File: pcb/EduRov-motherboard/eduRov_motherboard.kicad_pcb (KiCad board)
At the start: 4 copper layers, 167.7 x 124.6 mm, 65 parts, among them IC201 L6203, IC301 L6203, IC401 L6203, IC501 L6203, P101 Battery connector, P102 Ext press, P103 Ext press, P104 Ext press, P105 Ch LED, Q101 IRL540NPBF, U201 ACS723xLCTR-05AB, U301 ACS723xLCTR-05AB, U401 ACS723xLCTR-05AB, U501 ACS723xLCTR-05AB

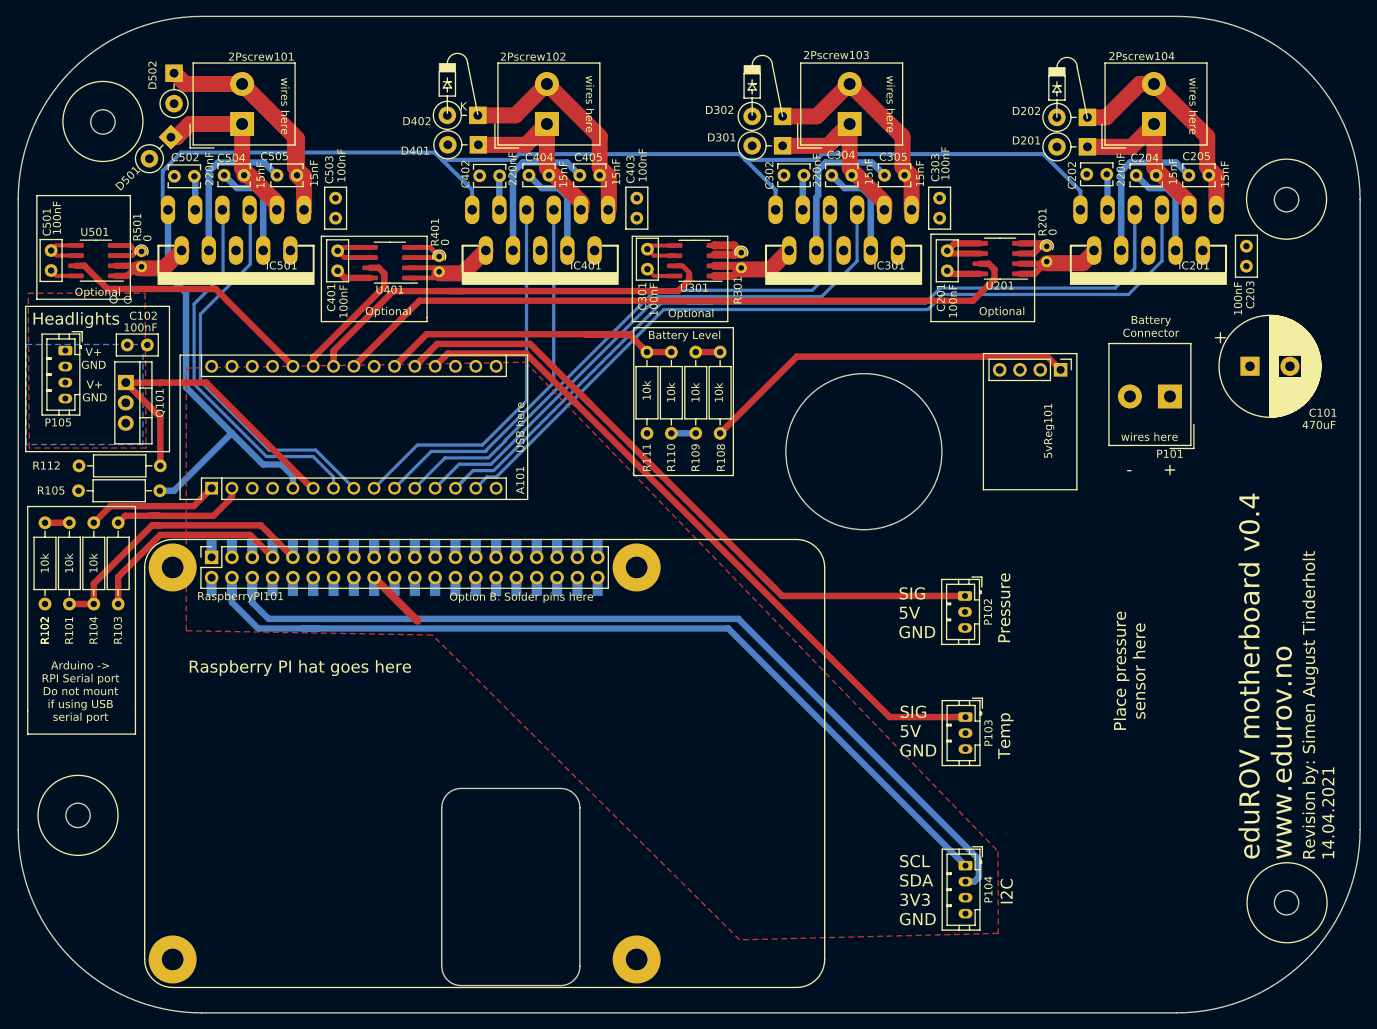
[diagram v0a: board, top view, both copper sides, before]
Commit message: Use L298 motor driver
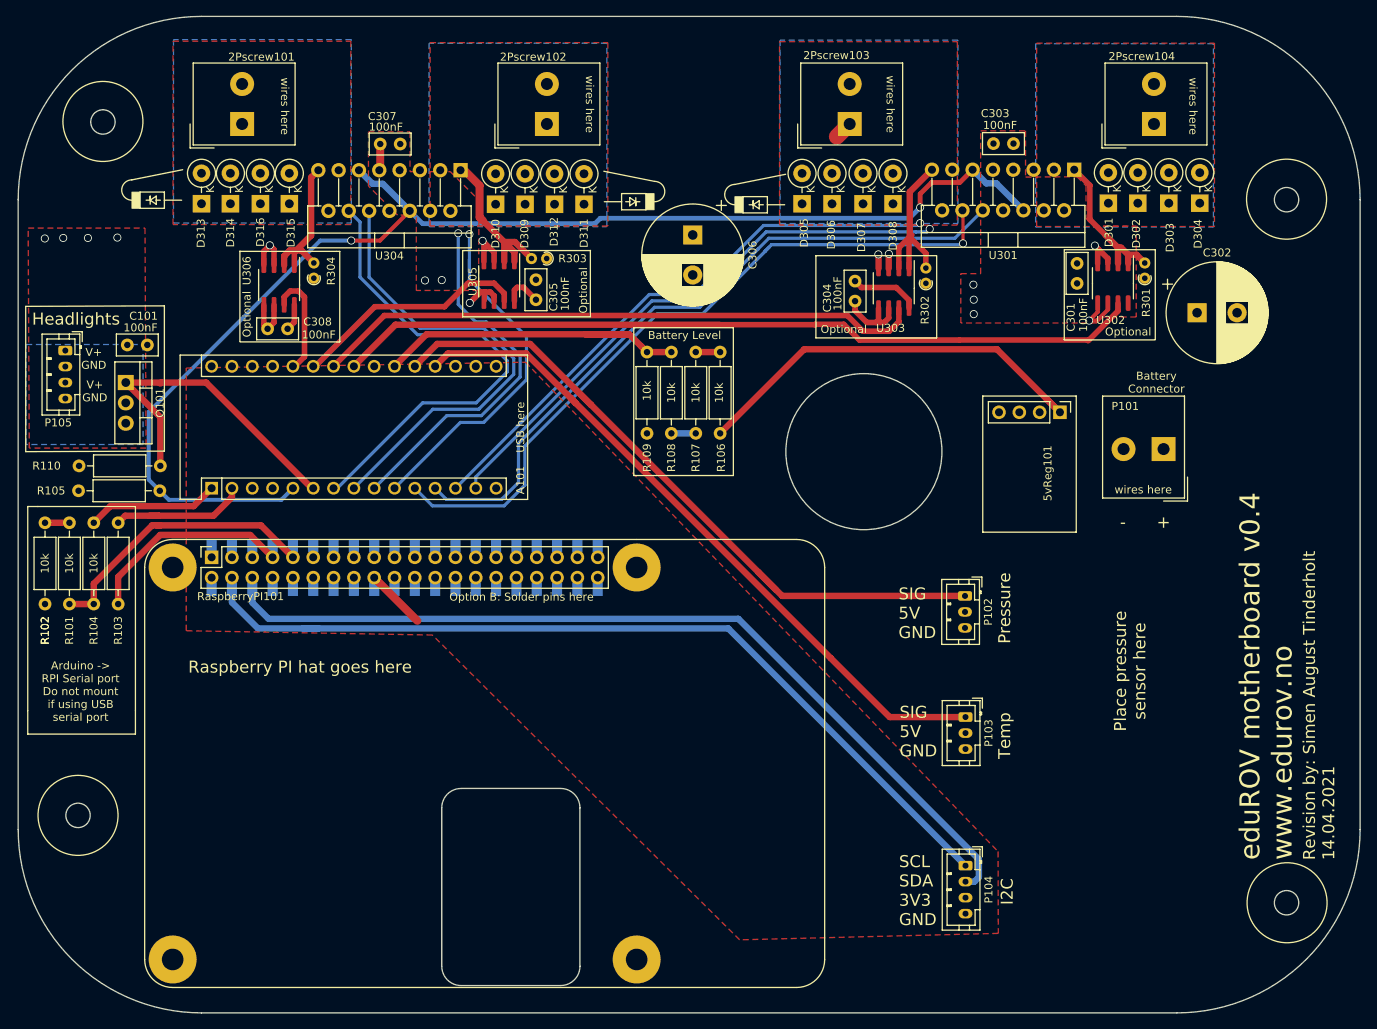
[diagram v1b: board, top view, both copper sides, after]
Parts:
- removed the C101 at (209.8, 76.7)
- removed C201, C203, C401, C403, C501, C503: 100nF, Capacitor_THT:C_Disc_D5.0mm_W2.5mm_P2.50mm
- removed C202, C402, C502: 220nF, Capacitor_THT:C_Disc_D3.8mm_W2.6mm_P2.50mm
- removed C204, C205, C404, C405, C504, C505: 15nF, Capacitor_THT:C_Disc_D3.8mm_W2.6mm_P2.50mm
- removed D201, D202, D401, D402, D501, D502: D, Diode_THT:D_DO-41_SOD81_P3.81mm_Vertical_KathodeUp
- removed IC201, IC301, IC401, IC501: L6203, SnapEDA Library:MULTIWATT-11
- removed R201, R401, R501: 0, Resistor_THT:R_Axial_DIN0204_L3.6mm_D1.6mm_P1.90mm_Vertical
- removed U201, U401, U501: ACS723xLCTR-05AB, Package_SO:SOIC-8_3.9x4.9mm_P1.27mm
- added C306: 470uF, Capacitor_THT:CP_Radial_D12.5mm_P5.00mm, F.Cu at (140.1, 60.3)
- added C307: 100nF, Capacitor_THT:C_Disc_D5.0mm_W2.5mm_P2.50mm, F.Cu at (103.6, 48.9)
- added C308: 100nF, Capacitor_THT:C_Disc_D5.0mm_W2.5mm_P2.50mm, F.Cu at (87.0, 72.0)
- added D303: D, Diode_THT:D_DO-41_SOD81_P3.81mm_Vertical_KathodeUp, F.Cu at (199.7, 56.3)
- added D304: D, Diode_THT:D_DO-41_SOD81_P3.81mm_Vertical_KathodeUp, F.Cu at (203.5, 56.3)
- added D305: D, Diode_THT:D_DO-41_SOD81_P3.81mm_Vertical_KathodeUp, F.Cu at (153.8, 56.4)
- added D306: D, Diode_THT:D_DO-41_SOD81_P3.81mm_Vertical_KathodeUp, F.Cu at (157.6, 56.4)
- added D307: D, Diode_THT:D_DO-41_SOD81_P3.81mm_Vertical_KathodeUp, F.Cu at (161.4, 56.4)
- added D308: D, Diode_THT:D_DO-41_SOD81_P3.81mm_Vertical_KathodeUp, F.Cu at (165.2, 56.4)
- added D309: D, Diode_THT:D_DO-41_SOD81_P3.81mm_Vertical_KathodeUp, F.Cu at (119.2, 56.5)
- added D310: D, Diode_THT:D_DO-41_SOD81_P3.81mm_Vertical_KathodeUp, F.Cu at (115.5, 56.5)
- added D311: D, Diode_THT:D_DO-41_SOD81_P3.81mm_Vertical_KathodeUp, F.Cu at (126.6, 56.5)
- added D312: D, Diode_THT:D_DO-41_SOD81_P3.81mm_Vertical_KathodeUp, F.Cu at (122.9, 56.5)
- added D313: D, Diode_THT:D_DO-41_SOD81_P3.81mm_Vertical_KathodeUp, F.Cu at (78.7, 56.4)
- added D314: D, Diode_THT:D_DO-41_SOD81_P3.81mm_Vertical_KathodeUp, F.Cu at (82.4, 56.4)
- added D315: D, Diode_THT:D_DO-41_SOD81_P3.81mm_Vertical_KathodeUp, F.Cu at (89.7, 56.4)
- added D316: D, Diode_THT:D_DO-41_SOD81_P3.81mm_Vertical_KathodeUp, F.Cu at (86.1, 56.4)
- added R302: 0, Resistor_THT:R_Axial_DIN0204_L3.6mm_D1.6mm_P1.90mm_Vertical, F.Cu at (169.3, 66.3)
- added R303: 0, Resistor_THT:R_Axial_DIN0204_L3.6mm_D1.6mm_P1.90mm_Vertical, F.Cu at (121.9, 63.2)
- added R304: 0, Resistor_THT:R_Axial_DIN0204_L3.6mm_D1.6mm_P1.90mm_Vertical, F.Cu at (92.8, 65.7)
- added U302: ACS723xLCTR-05AB, Package_SO:SOIC-8_3.9x4.9mm_P1.27mm, F.Cu at (192.7, 66.3)
- added U303: ACS723xLCTR-05AB, Package_SO:SOIC-8_3.9x4.9mm_P1.27mm, F.Cu at (165.3, 67.0)
- added U304: L298HN, Package_TO_SOT_THT:TO-220-15_P2.54x2.54mm_StaggerOdd_Lead4.58mm_Vertical, F.Cu at (111.1, 52.2)
- added U305: ACS723xLCTR-05AB, Package_SO:SOIC-8_3.9x4.9mm_P1.27mm, F.Cu at (116.0, 66.1)
- added U306: ACS723xLCTR-05AB, Package_SO:SOIC-8_3.9x4.9mm_P1.27mm, F.Cu at (88.4, 66.5)
- C302: value 220nF -> 470uF; footprint Capacitor_THT:C_Disc_D3.8mm_W2.6mm_P2.50mm -> Capacitor_THT:CP_Radial_D12.5mm_P5.00mm
- C304, C305: value 15nF -> 100nF; footprint Capacitor_THT:C_Disc_D3.8mm_W2.6mm_P2.50mm -> Capacitor_THT:C_Disc_D5.0mm_W2.5mm_P2.50mm
- U301: value ACS723xLCTR-05AB -> L298HN; footprint Package_SO:SOIC-8_3.9x4.9mm_P1.27mm -> Package_TO_SOT_THT:TO-220-15_P2.54x2.54mm_StaggerOdd_Lead4.58mm_Vertical
- moved C301 53.9 mm to (188.2, 66.3), turned to 90 degrees
- moved C302 52.1 mm to (203.2, 70.0), turned to 0 degrees
- moved R301 50.5 mm to (196.7, 65.7), turned to 90 degrees
- moved U301 48.8 mm to (187.8, 52.1)
- moved C305 47.9 mm to (120.5, 65.9), turned to 270 degrees
- moved D302 45.7 mm to (195.8, 56.3), turned to 90 degrees
- moved D301 41.3 mm to (192.1, 56.3), turned to 90 degrees
- moved C304 15.7 mm to (160.4, 68.6), turned to 90 degrees
- moved C303 11.5 mm to (180.2, 48.9), turned to 180 degrees
- moved P101 6.62 mm to (199.0, 87.1)
- moved 5vReg101 5.30 mm to (186.0, 82.5)
- renumbered C102 to C101, R108 to R106, R109 to R107, R110 to R108, R111 to R109, R112 to R110
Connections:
- C302 pad 1: Net-(C302-Pad1) -> +Bat
- C303 pad 2: +Bat -> +5V
- C304 pad 1: /Mot3- -> -Batt
- C304 pad 2: Net-(C304-Pad2) -> +5V
- C305 pad 1: /Mot3+ -> -Batt
- C305 pad 2: Net-(C305-Pad2) -> +5V
- D301 pad 1: /Mot3- -> +Bat
- D301 pad 2: -Batt -> /Mot4-
- D302 pad 1: /Mot3+ -> /Mot4-
- P101 pad 1: Net-(P101-Pad1) -> +Bat
- R301 pad 2: Net-(IC301-Pad10) -> /MotorController2/IA
- U301 pad 1: Net-(IC301-Pad10) -> /MotorController2/IA
- U301 pad 2: Net-(IC301-Pad10) -> /Mot4-
- U301 pad 3: -Batt -> /Mot4+
- U301 pad 4: -Batt -> +Bat
- U301 pad 5: -Batt -> IO4A
- U301 pad 6: -Batt -> IOEN
- U301 pad 7: Sense3 -> IO4B
- U301 pad 8: +5V -> -Batt
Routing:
- net /Mot1+: track 46.4 -> 0.00 mm
- net IOEN: track 197.3 -> 162.9 mm, vias 0 -> 2
- net /Mot2+: track 29.2 -> 0.00 mm
- net /Mot3+: track 29.0 -> 0.00 mm
- net /Mot4+: track 29.0 -> 0.00 mm
- net /Mot1-: track 28.4 -> 0.00 mm
- net /Mot2-: track 24.5 -> 0.00 mm
- net /MotorController2/IB: track 0.00 -> 23.4 mm
- net /Mot4-: track 22.1 -> 0.00 mm
- net /Mot3-: track 24.3 -> 2.27 mm
- net Sense3: track 54.9 -> 76.3 mm
- net /MotorController1/IA: track 0.00 -> 21.2 mm
- net IO3B: track 71.0 -> 90.8 mm, vias 0 -> 1
- net Net-(C505-Pad2): track 19.5 -> 0.00 mm
- net Net-(C305-Pad2): track 19.5 -> 0.00 mm
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- added copper zone on F.Cu, net +5V
- added copper zone on B.Cu, net /Mot1+
- added copper zone on F.Cu, net /Mot1-
- added copper zone on F.Cu, net /Mot2+
- added copper zone on B.Cu, net /Mot2-
- added copper zone on B.Cu, net /Mot3+
- added copper zone on F.Cu, net /Mot3-
- added copper zone on F.Cu, net /Mot4+
- added copper zone on B.Cu, net /Mot4-
